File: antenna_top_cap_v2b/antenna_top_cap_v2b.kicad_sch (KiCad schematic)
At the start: 32 parts, among them J1 DEBUG, J12 USB_C_Receptacle_USB2.0_16P, J2 Battery Charge Bypass, J3 FC Reset Jumper, J4 FC USB Bootselect Jumper, J5 Conn_Coaxial, Q1 BSS138, U1 VL6180XV0NR/1, U16 MCP9808T-E/MS, U2 LP5907-2.8V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

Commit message: Added Payload USB Passthrough
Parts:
- added J8: USB_C_Receptacle_USB2.0_16P, Connector_USB:USB_C_Receptacle_HRO_TYPE-C-31-M-12, symbol Connector:USB_C_Receptacle_USB2.0_16P
- added J9: Conn_02x02_Odd_Even, Connector_Hirose:Hirose_DF11-4DP-2DSA_2x02_P2.00mm_Vertical, symbol Connector_Generic:Conn_02x02_Odd_Even
- added R5, R6: 5.1k, Resistor_SMD:R_0603_1608Metric, symbol mainboard:RESISTOR0603
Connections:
- net GND: now also J8.A1 (GND), J8.A12 (GND), J8.B1 (GND), J8.B12 (GND), J8.S1 (SHIELD), J9.4 (Pin_4), R5.1, R6.1
- new net: J8.A5 (CC1), R5.2
- new net: J8.B5 (CC2), R6.2
- new net Payload_D+: J8.A6 (D+), J8.B6 (D+), J9.3 (Pin_3)
- new net Payload_D-: J8.A7 (D-), J8.B7 (D-), J9.1 (Pin_1)
- new net Payload_VBUS: J8.A4 (VBUS), J8.A9 (VBUS), J8.B4 (VBUS), J8.B9 (VBUS), J9.2 (Pin_2)
- no-connect marks 13 -> 15
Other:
- note added: "FC Board Connection"
- note added: "Payload Board Connection"
- moved on the sheet: J12, R26, R27

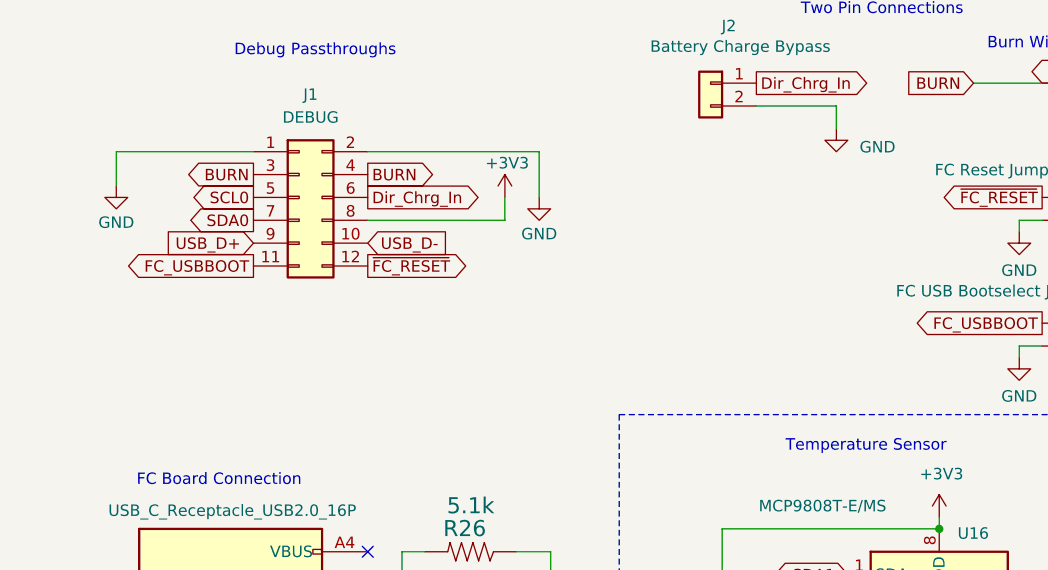
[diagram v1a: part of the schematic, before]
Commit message: Redid USB Trace Impedance
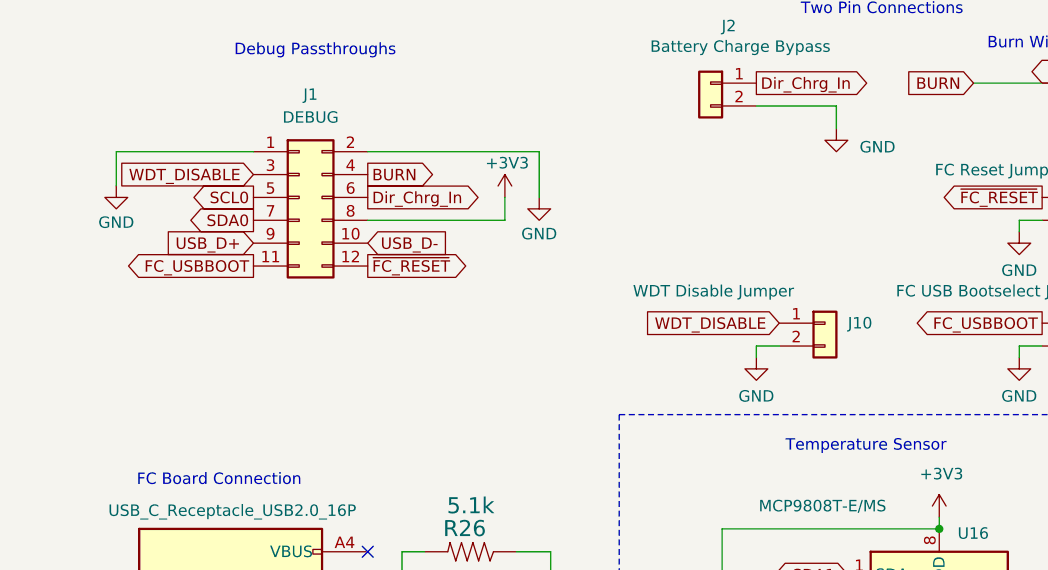
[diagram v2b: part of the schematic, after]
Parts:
- added J10: WDT Disable Jumper, Connector_PinHeader_2.54mm:PinHeader_1x02_P2.54mm_Vertical, symbol Connector_Generic:Conn_01x02
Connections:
- net BURN: no longer J1.3 (Pin_3)
- net GND: now also J10.2 (Pin_2)
- new net WDT_DISABLE: J1.3 (Pin_3), J10.1 (Pin_1)
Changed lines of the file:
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@@
 	(wire
 		(pts
+			(xy 92.71 50.8) (xy 92.71 52.07)
+		)
+		(stroke
+			(width 0)
+			(type default)
+		)
+	)
+	(wire
+		(pts
 			(xy 46.99 154.94) (xy 59.69 154.94)
 		)
@@
 	(wire
 		(pts
+			(xy 95.25 50.8) (xy 92.71 50.8)
+		)
+		(stroke
+			(width 0)
+			(type default)
+		)
+	)
+	(wire
+		(pts
 			(xy 180.34 45.72) (xy 170.18 45.72)
 		)
@@
 		)
 	)
-	(global_label "BURN"
-		(shape output)
-		(at 36.83 31.75 180)
+	(global_label "WDT_DISABLE"
+		(shape input)
+		(at 95.25 48.26 180)
 		(fields_autoplaced yes)
 		(effects
@@
 		)
 		(property "Intersheetrefs" "${INTERSHEET_REFS}"
-			(at 28.6438 31.75 0)
+			(at 79.9882 48.26 0)
 			(effects
 				(font
@@
 		)
 	)
+	(global_label "WDT_DISABLE"
+		(shape input)
+		(at 36.83 31.75 180)
+		(fields_autoplaced yes)
+		(effects
+			(font
+				(size 1.27 1.27)
+			)
+			(justify right)
+		)
+		(property "Intersheetrefs" "${INTERSHEET_REFS}"
+			(at 21.5682 31.75 0)
+			(effects
+				(font
+					(size 1.27 1.27)
+				)
+				(justify right)
+				(hide yes)
+			)
+		)
+	)
 	(global_label "USB_D+"
 		(shape input)
@@
 	)
 	(symbol
+		(lib_id "Connector_Generic:Conn_01x02")
+		(at 100.33 48.26 0)
+		(unit 1)
+		(exclude_from_sim no)
+		(in_bom yes)
+		(on_board yes)
+		(dnp no)
+		(property "Reference" "J10"
+			(at 102.87 48.2599 0)
+			(effects
+				(font
+					(size 1.27 1.27)
+				)
+				(justify left)
+			)
+		)
+		(property "Value" "WDT Disable Jumper"
+			(at 78.994 44.704 0)
+			(effects
+				(font
+					(size 1.27 1.27)
+				)
+				(justify left)
+			)
+		)
+		(property "Footprint" "Connector_PinHeader_2.54mm:PinHeader_1x02_P2.54mm_Vertical"
+			(at 100.33 48.26 0)
+			(effects
+				(font
+					(size 1.27 1.27)
+				)
+				(hide yes)
+			)
+		)
+		(property "Datasheet" "~"
+			(at 100.33 48.26 0)
+			(effects
+				(font
+					(size 1.27 1.27)
+				)
+				(hide yes)
+			)
+		)
+		(property "Description" "Generic connector, single row, 01x02, script generated (kicad-library-utils/schlib/autogen/connector/)"
+			(at 100.33 48.26 0)
+			(effects
+				(font
+					(size 1.27 1.27)
+				)
+				(hide yes)
+			)
+		)
+		(pin "1"
+		)
+		(pin "2"
+		)
+		(instances
+			(project "antenna_top_cap_v2b"
+				(path "/e63e39d7-6ac0-4ffd-8aa3-1841a4541b55"
+					(reference "J10")
+					(unit 1)
+				)
+			)
+		)
+	)
+	(symbol
 		(lib_id "solar-panel-side-Z-rescue:+3.3V-power")
 		(at 113.03 69.85 0)
@@
 					(unit 1)
 				)
+			)
+		)
+	)
+	(symbol
+		(lib_name "GND_1")
+		(lib_id "power:GND")
+		(at 92.71 52.07 0)
+		(unit 1)
+		(exclude_from_sim no)
+		(in_bom yes)
+		(on_board yes)
+		(dnp no)
+		(property "Reference" "#PWR06"
+			(at 92.71 58.42 0)
+			(effects
+				(font
+					(size 1.27 1.27)
+				)
+				(hide yes)
+			)
+		)
+		(property "Value" "GND"
+			(at 92.71 56.388 0)
+			(effects
+				(font
+					(size 1.27 1.27)
+				)
+			)
+		)
+		(property "Footprint" ""
+			(at 92.71 52.07 0)
+			(effects
+				(font
+					(size 1.27 1.27)
+				)
+				(hide yes)
+			)
+		)
+		(property "Datasheet" ""
+			(at 92.71 52.07 0)
+			(effects
+				(font
+					(size 1.27 1.27)
+				)
+				(hide yes)
+			)
+		)
+		(property "Description" "Power symbol creates a global label with name \"GND\" , ground"
+			(at 92.71 52.07 0)
+			(effects
+				(font
+					(size 1.27 1.27)
+				)
+				(hide yes)
+			)
+		)
+		(pin "1"
+		)
+		(instances
+			(project "antenna_top_cap_v2b"
+				(path "/e63e39d7-6ac0-4ffd-8aa3-1841a4541b55"
+					(reference "#PWR06")
+					(unit 1)
+				)

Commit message: Added Alt RBF
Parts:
- added C4, C5: 100nF, Capacitor_SMD:C_0805_2012Metric, symbol Device:C
- added J11: DF11-4DP-2DSA, Connector_Hirose:Hirose_DF11-4DP-2DSA_2x02_P2.00mm_Vertical, symbol Connector_Generic:Conn_02x02_Odd_Even
- added J13: DNP, Connector_Hirose:Hirose_DF11-4DP-2DSA_2x02_P2.00mm_Vertical, symbol Connector_Generic:Conn_02x02_Odd_Even
- added Q2: CSD17576Q5B, Package_TO_SOT_SMD:TDSON-8-1, symbol Transistor_FET:CSD17576Q5B
- added R7: 1M, Resistor_SMD:R_0603_1608Metric, symbol mainboard:RESISTOR0603
- C43: value 1uF -> 100nF
- J9: value Conn_02x02_Odd_Even -> DF11-4DP-2DSA
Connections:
- net +3V3: now also C5.1
- net 2.8V: now also C4.1
- net GND: now also C4.2, C5.2, J13.2 (Pin_2), J13.4 (Pin_4)
- new net: J13.1 (Pin_1), J13.3 (Pin_3), Q2.4 (G), R7.1
- new net RBF_High: J11.1 (Pin_1), J11.3 (Pin_3), Q2.5 (D), R7.2
- new net RBF_Low: J11.2 (Pin_2), J11.4 (Pin_4), Q2.1 (S), Q2.2 (S), Q2.3 (S)
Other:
- note added: "RBF_ALT"
- moved on the sheet: J5, J6, U5
